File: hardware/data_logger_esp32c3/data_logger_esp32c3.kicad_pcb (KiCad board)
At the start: 2 copper layers, 43.4 x 55.4 mm, 48 parts, among them U1 ESP32-C3-MINI-1, U10 A03401A, U2 AZ1117IH-3.3TRG1, U3 LM321MF, U4 LM321MF, U5 LM321MF, U6 LM321MF, U7 LM321MF, U8 LM321MF, U9 A03401A

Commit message: More hardware work
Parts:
- moved U9 59.2 mm to (134.9, 88.2)
- moved U10 58.3 mm to (137.7, 82.5)
- moved TX0 19.3 mm to (124.7, 51.6)
- moved R1 14.5 mm to (126.4, 56.9), turned to 90 degrees
- moved RX0 14.4 mm to (124.7, 54.5)
- moved C3 11.3 mm to (106.4, 57.6), turned to 180 degrees
- moved R3 10.4 mm to (126.4, 54.9), turned to -90 degrees
- moved C1 2.82 mm to (105.9, 63.2), turned to -90 degrees
- moved R7 2.28 mm to (131.7, 69.1)
- moved U1 2.11 mm to (116.7, 58.2)
- moved SD1 1.63 mm to (134.1, 69.4)
- moved C2 1.06 mm to (106.1, 58.9), turned to 180 degrees
- moved R2 1.02 mm to (131.7, 72.0)
- moved USB-C1 0.88 mm to (129.1, 70.0)
- moved R4 0.83 mm to (107.1, 63.2), turned to 90 degrees
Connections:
- U1 pad 11: (no net) -> GND
- U1 pad 14: (no net) -> GND

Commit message: adding to hardware
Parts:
- added ?: TestPoint, TestPoint:TestPoint_THTPad_1.0x1.0mm_Drill0.5mm, F.Cu at (127.3, 76.1)
- added ?: TestPoint, TestPoint:TestPoint_THTPad_1.0x1.0mm_Drill0.5mm, F.Cu at (124.3, 76.1)
- moved ADC1-1 55.6 mm to (114.7, 75.8)
- moved ADC1+1 53.3 mm to (108.6, 75.9)
- moved U4 47.4 mm to (110.6, 65.8)
- moved C5 22.6 mm to (141.3, 79.7), turned to 90 degrees
- moved U2 16.8 mm to (136.8, 87.8), turned to 180 degrees
- moved U9 15.7 mm to (128.0, 74.2)
- moved U10 14.8 mm to (131.4, 69.1)
- moved DC-1 13.9 mm to (126.3, 83.4)
- moved R9 12.4 mm to (131.4, 76.7)
- moved DC+1 11.6 mm to (123.5, 83.4)
- moved C4 11.1 mm to (131.5, 78.1)
- moved D1 9.95 mm to (130.5, 79.4), turned to -90 degrees
- moved 3V3 7.06 mm to (140.6, 84.2)
- moved VIN1 6.45 mm to (131.6, 79.9)
- moved C3 2.86 mm to (109.2, 57.3), turned to 90 degrees
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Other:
- board size 43.4 x 55.4 mm -> 50 x 50 mm

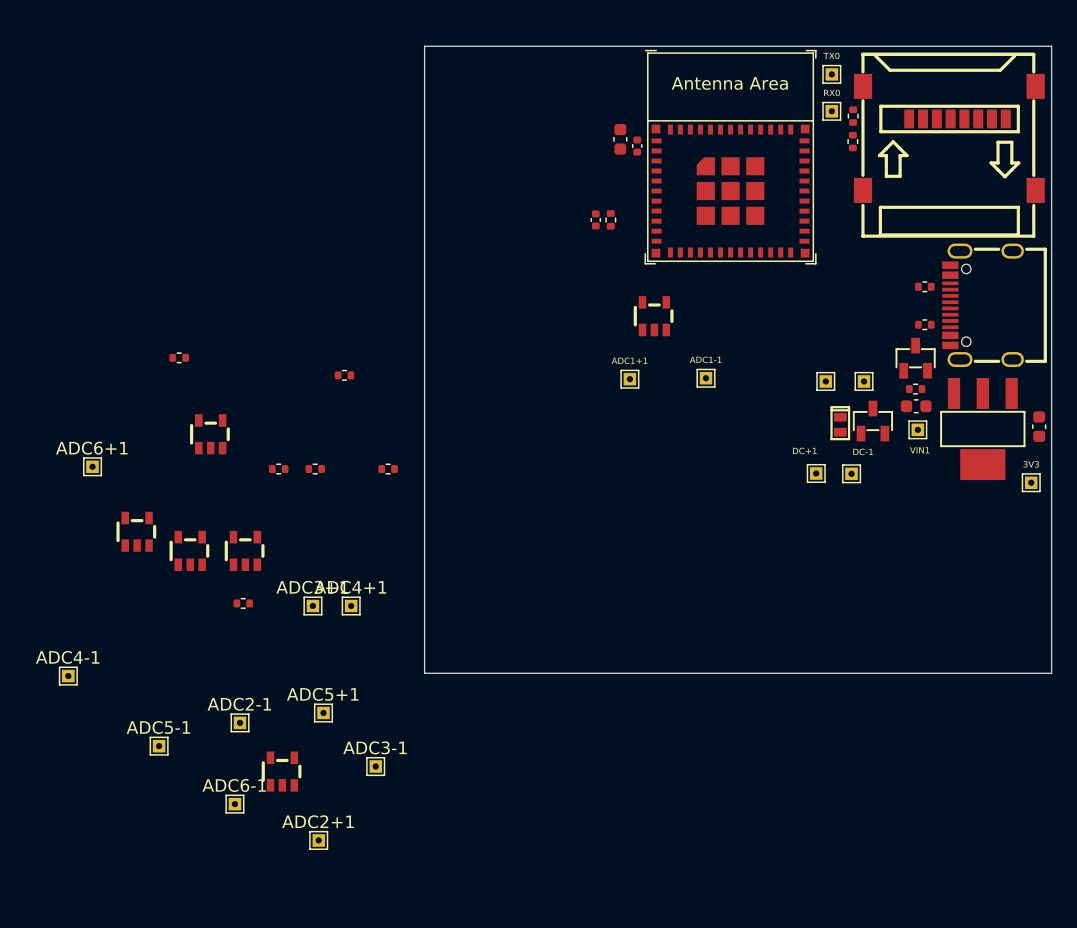
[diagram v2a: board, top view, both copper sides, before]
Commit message: Add gpio expander.  Layout complete
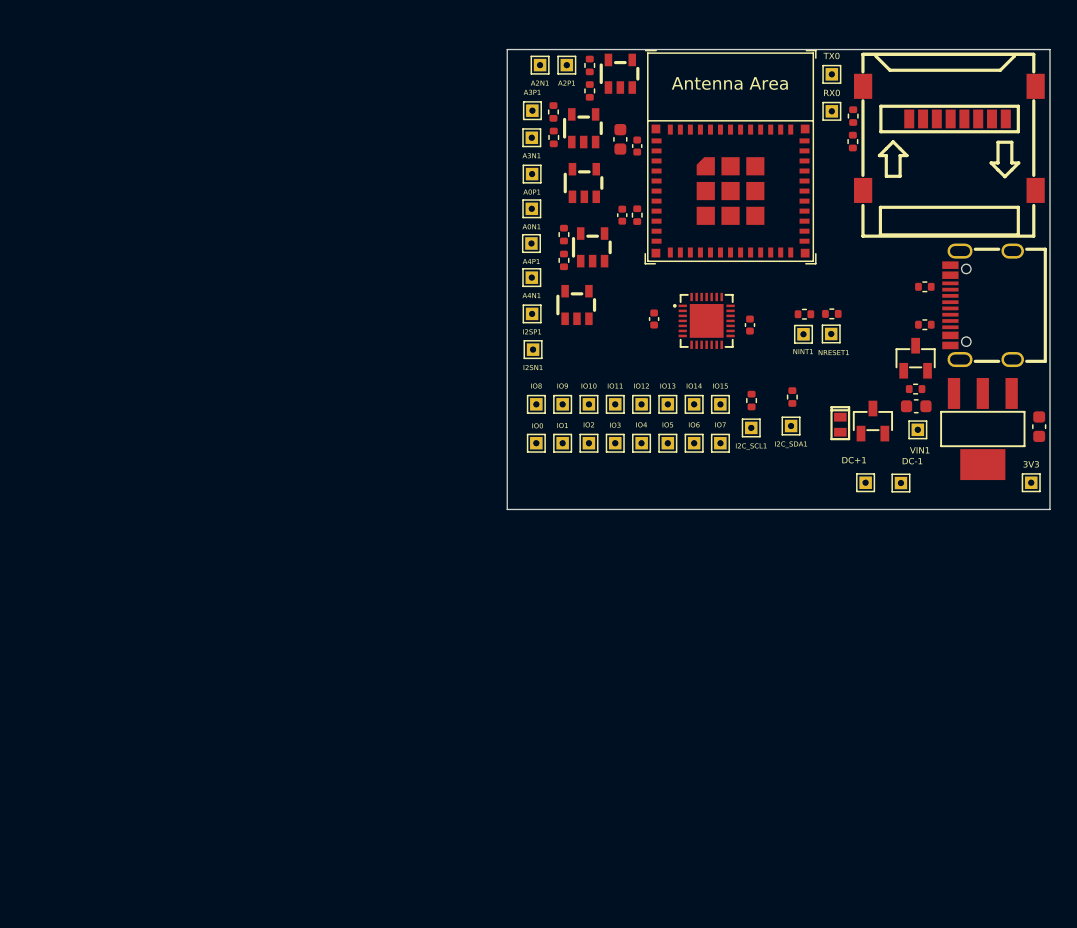
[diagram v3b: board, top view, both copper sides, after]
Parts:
- removed ? (x2), ADC1+1, ADC1-1, ADC2+1, ADC2-1, ADC3+1, ADC3-1, ADC4+1, ADC4-1, ADC5+1, ADC5-1, ADC6+1, ADC6-1: TestPoint, TestPoint:TestPoint_THTPad_1.0x1.0mm_Drill0.5mm
- removed U3: LM321MF, 1_project_footprints:LM321MF
- added A0N1: TestPoint, TestPoint:TestPoint_THTPad_1.0x1.0mm_Drill0.5mm, F.Cu at (100.8, 62.3)
- added A0P1: TestPoint, TestPoint:TestPoint_THTPad_1.0x1.0mm_Drill0.5mm, F.Cu at (100.8, 59.5)
- added A2N1: TestPoint, TestPoint:TestPoint_THTPad_1.0x1.0mm_Drill0.5mm, F.Cu at (101.5, 50.9)
- added A2P1: TestPoint, TestPoint:TestPoint_THTPad_1.0x1.0mm_Drill0.5mm, F.Cu at (103.6, 50.9)
- added A3N1: TestPoint, TestPoint:TestPoint_THTPad_1.0x1.0mm_Drill0.5mm, F.Cu at (100.8, 56.6)
- added A3P1: TestPoint, TestPoint:TestPoint_THTPad_1.0x1.0mm_Drill0.5mm, F.Cu at (100.9, 54.5)
- added A4N1: TestPoint, TestPoint:TestPoint_THTPad_1.0x1.0mm_Drill0.5mm, F.Cu at (100.8, 67.8)
- added A4P1: TestPoint, TestPoint:TestPoint_THTPad_1.0x1.0mm_Drill0.5mm, F.Cu at (100.8, 65.1)
- added C6: 0.1uF, Capacitor_SMD:C_0402_1005Metric, F.Cu at (118.2, 71.6)
- added C7: 0.1uF, Capacitor_SMD:C_0402_1005Metric, F.Cu at (110.6, 71.1)
- added I2C_SCL1: TestPoint, TestPoint:TestPoint_THTPad_1.0x1.0mm_Drill0.5mm, F.Cu at (118.3, 79.8)
- added I2C_SDA1: TestPoint, TestPoint:TestPoint_THTPad_1.0x1.0mm_Drill0.5mm, F.Cu at (121.5, 79.6)
- added I2SN1: TestPoint, TestPoint:TestPoint_THTPad_1.0x1.0mm_Drill0.5mm, F.Cu at (100.9, 73.5)
- added I2SP1: TestPoint, TestPoint:TestPoint_THTPad_1.0x1.0mm_Drill0.5mm, F.Cu at (100.8, 70.7)
- added IO0: TestPoint, TestPoint:TestPoint_THTPad_1.0x1.0mm_Drill0.5mm, F.Cu at (101.2, 81.0)
- added IO1: TestPoint, TestPoint:TestPoint_THTPad_1.0x1.0mm_Drill0.5mm, F.Cu at (103.3, 81.0)
- added IO10: TestPoint, TestPoint:TestPoint_THTPad_1.0x1.0mm_Drill0.5mm, F.Cu at (105.4, 77.9)
- added IO11: TestPoint, TestPoint:TestPoint_THTPad_1.0x1.0mm_Drill0.5mm, F.Cu at (107.5, 77.9)
- added IO12: TestPoint, TestPoint:TestPoint_THTPad_1.0x1.0mm_Drill0.5mm, F.Cu at (109.6, 77.9)
- added IO13: TestPoint, TestPoint:TestPoint_THTPad_1.0x1.0mm_Drill0.5mm, F.Cu at (111.7, 77.9)
- added IO14: TestPoint, TestPoint:TestPoint_THTPad_1.0x1.0mm_Drill0.5mm, F.Cu at (113.8, 77.9)
- added IO15: TestPoint, TestPoint:TestPoint_THTPad_1.0x1.0mm_Drill0.5mm, F.Cu at (115.9, 77.9)
- added IO2: TestPoint, TestPoint:TestPoint_THTPad_1.0x1.0mm_Drill0.5mm, F.Cu at (105.4, 81.0)
- added IO3: TestPoint, TestPoint:TestPoint_THTPad_1.0x1.0mm_Drill0.5mm, F.Cu at (107.5, 81.0)
- added IO4: TestPoint, TestPoint:TestPoint_THTPad_1.0x1.0mm_Drill0.5mm, F.Cu at (109.6, 81.0)
- added IO5: TestPoint, TestPoint:TestPoint_THTPad_1.0x1.0mm_Drill0.5mm, F.Cu at (111.7, 81.0)
- added IO6: TestPoint, TestPoint:TestPoint_THTPad_1.0x1.0mm_Drill0.5mm, F.Cu at (113.8, 81.0)
- added IO7: TestPoint, TestPoint:TestPoint_THTPad_1.0x1.0mm_Drill0.5mm, F.Cu at (115.9, 81.0)
- added IO8: TestPoint, TestPoint:TestPoint_THTPad_1.0x1.0mm_Drill0.5mm, F.Cu at (101.2, 77.9)
- added IO9: TestPoint, TestPoint:TestPoint_THTPad_1.0x1.0mm_Drill0.5mm, F.Cu at (103.3, 77.9)
- added NINT1: TestPoint, TestPoint:TestPoint_THTPad_1.0x1.0mm_Drill0.5mm, F.Cu at (122.5, 72.3)
- added NRESET1: TestPoint, TestPoint:TestPoint_THTPad_1.0x1.0mm_Drill0.5mm, F.Cu at (124.7, 72.3)
- added R14: 10k, Resistor_SMD:R_0402_1005Metric, F.Cu at (124.7, 70.7)
- added R15: 10k, Resistor_SMD:R_0402_1005Metric, F.Cu at (122.6, 70.7)
- added R16: 4.7k, Resistor_SMD:R_0402_1005Metric, F.Cu at (121.6, 77.3)
- added R8: 4.7k, Resistor_SMD:R_0402_1005Metric, F.Cu at (118.3, 77.6)
- added U11: SX1509BIULTRT, 1_project_footprints:QFN-28-EP(4x4), F.Cu at (119.6, 71.2)
- moved R13 49.3 mm to (105.4, 52.9), turned to -90 degrees
- moved U5 48.4 mm to (107.9, 46.5)
- moved R10 40.6 mm to (105.4, 50.9), turned to -90 degrees
- moved U7 40.2 mm to (105.7, 60.3)
- moved U8 39.5 mm to (104.4, 64.9)
- moved U6 38.5 mm to (105.0, 50.8)
- moved R6 31.7 mm to (103.4, 66.4), turned to -90 degrees
- moved R11 31.4 mm to (102.5, 54.6), turned to -90 degrees
- moved R12 27.3 mm to (103.4, 64.4), turned to -90 degrees
- moved R5 25.3 mm to (102.6, 56.6), turned to -90 degrees
- moved U4 12.0 mm to (105.0, 55.2)
- moved DC-1 4.01 mm to (130.3, 84.2)
- moved DC+1 4.01 mm to (127.4, 84.2)
- moved C1 2.14 mm to (108.0, 62.8)
- moved R4 2.14 mm to (109.2, 62.8)
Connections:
- U1 pad 13: ADC1_CH1 -> I2C_SDA
- U1 pad 16: unconnected-(U1-Pad16) -> I2C_SCL
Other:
- board size 50 x 50 mm -> 43.3 x 36.7 mm

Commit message: more layout
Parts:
- removed I2C_SCL1, I2C_SDA1: TestPoint, TestPoint:TestPoint_THTPad_1.0x1.0mm_Drill0.5mm
- added SCL1: TestPoint, TestPoint:TestPoint_THTPad_1.0x1.0mm_Drill0.5mm, F.Cu at (117.7, 79.7)
- added SDA1: TestPoint, TestPoint:TestPoint_THTPad_1.0x1.0mm_Drill0.5mm, F.Cu at (119.9, 79.8)
- moved VIN1 14.9 mm to (126.5, 66.0)
- moved 3V3 13.4 mm to (127.9, 80.0)
- moved C5 13.2 mm to (129.0, 74.8)
- moved U2 12.9 mm to (124.6, 83.6)
- moved C4 12.2 mm to (129.8, 66.0), turned to 0 degrees
- moved DC+1 11.4 mm to (137.8, 79.5)
- moved DC-1 11.0 mm to (140.2, 79.5)
- moved D1 10.9 mm to (138.9, 72.4), turned to 0 degrees
- moved R9 9.40 mm to (129.7, 67.4), turned to 180 degrees
- moved U9 9.27 mm to (132.0, 82.5), turned to 180 degrees
- moved NINT1 5.96 mm to (117.4, 75.5)
- moved R14 5.96 mm to (119.7, 73.9)
- moved R15 5.96 mm to (117.5, 73.9)
- moved NRESET1 5.96 mm to (119.7, 75.5)
- moved U10 3.39 mm to (134.7, 70.1), turned to -90 degrees
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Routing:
- added copper zone on In1.Cu, net +3V3
- added copper zone on In2.Cu, net GND
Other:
- board size 43.3 x 36.7 mm -> 43.3 x 32.3 mm
- copper layers 2 -> 4

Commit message: commit before routing
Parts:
- added R17: 30.1, Resistor_SMD:R_0402_1005Metric, F.Cu at (124.6, 63.3)
- added R18: 30.1, Resistor_SMD:R_0402_1005Metric, F.Cu at (124.6, 64.4)
- moved VIN1 15.0 mm to (130.2, 80.5), turned to -90 degrees
- moved 3V3 0.43 mm to (127.9, 80.5)
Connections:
- USB-C1 pad A6: D+ -> Net-(USB-C1-PadA6)
- USB-C1 pad A7: D- -> Net-(USB-C1-PadA7)
- USB-C1 pad B6: D+ -> Net-(USB-C1-PadA6)
- USB-C1 pad B7: D- -> Net-(USB-C1-PadA7)
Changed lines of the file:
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@@
   (net 68 "Net-(A4P1-Pad1)")
   (net 69 "Net-(I2SP1-Pad1)")
+  (net 70 "Net-(USB-C1-PadA6)")
+  (net 71 "Net-(USB-C1-PadA7)")
   (footprint "1_project_footprints:LM321MF" (layer "F.Cu")
     (at 107.873813 46.456944)
@@
   )
   (footprint "TestPoint:TestPoint_THTPad_1.0x1.0mm_Drill0.5mm" (layer "F.Cu")
-    (at 126.5174 65.9638)
+    (at 130.175 80.518 -90)
     (descr "THT rectangular pad as test Point, square 1.0mm side length, hole diameter 0.5mm")
     (tags "test point THT pad rectangle square")
@@
     (property "Sheetname" "")
     (attr exclude_from_pos_files)
-    (fp_text reference "VIN1" (at -1.4986 0.0508 90) (layer "F.SilkS")
+    (fp_text reference "VIN1" (at -1.4986 0.0508) (layer "F.SilkS")
       (effects (font (size 0.5 0.5) (thickness 0.125)))
     )
-    (fp_text value "TestPoint" (at 0 1.55) (layer "F.Fab")
-      (effects (font (size 1 1) (thickness 0.15)))
-    )
-    (fp_text user "${REFERENCE}" (at 0 -1.45) (layer "F.Fab")
+    (fp_text value "TestPoint" (at 0 1.55 90) (layer "F.Fab")
+      (effects (font (size 1 1) (thickness 0.15)))
+    )
+    (fp_text user "${REFERENCE}" (at 0 -1.45 90) (layer "F.Fab")
       (effects (font (size 1 1) (thickness 0.15)))
     )
@@
     (fp_line (start 1 1) (end 1 -1) (layer "F.CrtYd") (width 0.05))
     (fp_line (start -1 -1) (end 1 -1) (layer "F.CrtYd") (width 0.05))
-    (pad "1" thru_hole rect (at 0 0) (size 1 1) (drill 0.5) (layers *.Cu *.Mask)
+    (pad "1" thru_hole rect (at 0 0 270) (size 1 1) (drill 0.5) (layers *.Cu *.Mask)
       (net 39 "Net-(C4-Pad1)") (pinfunction "1") (pintype "passive"))
   )
@@
   )
   (footprint "Resistor_SMD:R_0402_1005Metric" (layer "F.Cu")
+    (at 124.6124 64.3636)
+    (descr "Resistor SMD 0402 (1005 Metric), square (rectangular) end terminal, IPC_7351 nominal, (Body size source: IPC-SM-782 page 72, https://www.pcb-3d.com/wordpress/wp-content/uploads/ipc-sm-782a_amendment_1_and_2.pdf), generated with kicad-footprint-generator")
+    (tags "resistor")
+    (property "Sheetfile" "data_logger_esp32c3.kicad_sch")
+    (property "Sheetname" "")
+    (property "part_number" "0402WGF301JTCE")
+    (attr smd)
+    (fp_text reference "R18" (at -0.4572 0.9144) (layer "F.SilkS")
+      (effects (font (size 0.4 0.4) (thickness 0.1)))
+    )
+    (fp_text value "30.1" (at 0 1.17) (layer "F.Fab")
+      (effects (font (size 1 1) (thickness 0.15)))
+    )
+    (fp_text user "${REFERENCE}" (at 0 0) (layer "F.Fab")
+      (effects (font (size 0.26 0.26) (thickness 0.04)))
+    )
+    (fp_line (start -0.153641 -0.38) (end 0.153641 -0.38) (layer "F.SilkS") (width 0.12))
+    (fp_line (start -0.153641 0.38) (end 0.153641 0.38) (layer "F.SilkS") (width 0.12))
+    (fp_line (start 0.93 -0.47) (end 0.93 0.47) (layer "F.CrtYd") (width 0.05))
+    (fp_line (start -0.93 0.47) (end -0.93 -0.47) (layer "F.CrtYd") (width 0.05))
+    (fp_line (start -0.93 -0.47) (end 0.93 -0.47) (layer "F.CrtYd") (width 0.05))
+    (fp_line (start 0.93 0.47) (end -0.93 0.47) (layer "F.CrtYd") (width 0.05))
+    (fp_line (start -0.525 -0.27) (end 0.525 -0.27) (layer "F.Fab") (width 0.1))
+    (fp_line (start -0.525 0.27) (end -0.525 -0.27) (layer "F.Fab") (width 0.1))
+    (fp_line (start 0.525 -0.27) (end 0.525 0.27) (layer "F.Fab") (width 0.1))
+    (fp_line (start 0.525 0.27) (end -0.525 0.27) (layer "F.Fab") (width 0.1))
+    (pad "1" smd roundrect (at -0.51 0) (size 0.54 0.64) (layers "F.Cu" "F.Paste" "F.Mask") (roundrect_rratio 0.25)
+      (net 18 "D-") (pintype "passive"))
+    (pad "2" smd roundrect (at 0.51 0) (size 0.54 0.64) (layers "F.Cu" "F.Paste" "F.Mask") (roundrect_rratio 0.25)
+      (net 71 "Net-(USB-C1-PadA7)") (pintype "passive"))
+    (model "${KICAD6_3DMODEL_DIR}/Resistor_SMD.3dshapes/R_0402_1005Metric.wrl"
+      (offset (xyz 0 0 0))
+      (scale (xyz 1 1 1))
+      (rotate (xyz 0 0 0))
+    )
+  )
+  (footprint "Resistor_SMD:R_0402_1005Metric" (layer "F.Cu")
     (at 103.378 66.421 -90)
     (descr "Resistor SMD 0402 (1005 Metric), square (rectangular) end terminal, IPC_7351 nominal, (Body size source: IPC-SM-782 page 72, https://www.pcb-3d.com/wordpress/wp-content/uploads/ipc-sm-782a_amendment_1_and_2.pdf), generated with kicad-footprint-generator")
@@
     (pad "1" thru_hole rect (at 0 0 180) (size 1 1) (drill 0.5) (layers *.Cu *.Mask)
       (net 2 "GND") (pinfunction "1") (pintype "passive"))
+  )
+  (footprint "Resistor_SMD:R_0402_1005Metric" (layer "F.Cu")
+    (at 124.587 63.2714)
+    (descr "Resistor SMD 0402 (1005 Metric), square (rectangular) end terminal, IPC_7351 nominal, (Body size source: IPC-SM-782 page 72, https://www.pcb-3d.com/wordpress/wp-content/uploads/ipc-sm-782a_amendment_1_and_2.pdf), generated with kicad-footprint-generator")
+    (tags "resistor")
+    (property "Sheetfile" "data_logger_esp32c3.kicad_sch")
+    (property "Sheetname" "")
+    (property "part_number" "0402WGF301JTCE")
+    (attr smd)
+    (fp_text reference "R17" (at 0 -0.8636) (layer "F.SilkS")
+      (effects (font (size 0.4 0.4) (thickness 0.1)))
+    )
+    (fp_text value "30.1" (at 0 1.17) (layer "F.Fab")
+      (effects (font (size 1 1) (thickness 0.15)))
+    )
+    (fp_text user "${REFERENCE}" (at 0 0) (layer "F.Fab")
+      (effects (font (size 0.26 0.26) (thickness 0.04)))
+    )
+    (fp_line (start -0.153641 -0.38) (end 0.153641 -0.38) (layer "F.SilkS") (width 0.12))
+    (fp_line (start -0.153641 0.38) (end 0.153641 0.38) (layer "F.SilkS") (width 0.12))
+    (fp_line (start -0.93 0.47) (end -0.93 -0.47) (layer "F.CrtYd") (width 0.05))
+    (fp_line (start 0.93 0.47) (end -0.93 0.47) (layer "F.CrtYd") (width 0.05))
+    (fp_line (start -0.93 -0.47) (end 0.93 -0.47) (layer "F.CrtYd") (width 0.05))
+    (fp_line (start 0.93 -0.47) (end 0.93 0.47) (layer "F.CrtYd") (width 0.05))
+    (fp_line (start -0.525 -0.27) (end 0.525 -0.27) (layer "F.Fab") (width 0.1))
+    (fp_line (start -0.525 0.27) (end -0.525 -0.27) (layer "F.Fab") (width 0.1))
+    (fp_line (start 0.525 0.27) (end -0.525 0.27) (layer "F.Fab") (width 0.1))
+    (fp_line (start 0.525 -0.27) (end 0.525 0.27) (layer "F.Fab") (width 0.1))
+    (pad "1" smd roundrect (at -0.51 0) (size 0.54 0.64) (layers "F.Cu" "F.Paste" "F.Mask") (roundrect_rratio 0.25)
+      (net 17 "D+") (pintype "passive"))
+    (pad "2" smd roundrect (at 0.51 0) (size 0.54 0.64) (layers "F.Cu" "F.Paste" "F.Mask") (roundrect_rratio 0.25)
+      (net 70 "Net-(USB-C1-PadA6)") (pintype "passive"))
+    (model "${KICAD6_3DMODEL_DIR}/Resistor_SMD.3dshapes/R_0402_1005Metric.wrl"
+      (offset (xyz 0 0 0))
+      (scale (xyz 1 1 1))
+      (rotate (xyz 0 0 0))
+    )
   )
   (footprint "1_espressif:ESP32-C3-MINI-1" (layer "F.Cu")
@@
   )
   (footprint "TestPoint:TestPoint_THTPad_1.0x1.0mm_Drill0.5mm" (layer "F.Cu")
-    (at 127.9144 80.0354)
+    (at 127.9144 80.4672)
     (descr "THT rectangular pad as test Point, square 1.0mm side length, hole diameter 0.5mm")
     (tags "test point THT pad rectangle square")
@@
       (net 36 "Net-(R2-Pad2)") (pinfunction "CC1") (pintype "bidirectional"))
     (pad "A6" smd rect (at -0.249936 5.13588 90) (size 0.299999 1.299997) (layers "F.Cu" "F.Paste" "F.Mask")
-      (net 17 "D+") (pinfunction "DP1") (pintype "bidirectional"))
+      (net 70 "Net-(USB-C1-PadA6)") (pinfunction "DP1") (pintype "bidirectional"))
     (pad "A7" smd rect (at 0.249936 5.13588 90) (size 0.299999 1.299997) (layers "F.Cu" "F.Paste" "F.Mask")
-      (net 18 "D-") (pinfunction "DN1") (pintype "bidirectional"))
+      (net 71 "Net-(USB-C1-PadA7)") (pinfunction "DN1") (pintype "bidirectional"))
     (pad "A8" smd rect (at 1.24968 5.13588 90) (size 0.299999 1.299997) (layers "F.Cu" "F.Paste" "F.Mask")
       (net 19 "unconnected-(USB-C1-PadA8)") (pinfunction "SBU1") (pintype "bidirectional+no_connect"))
@@
       (net 37 "Net-(R7-Pad2)") (pinfunction "CC2") (pintype "bidirectional"))
     (pad "B6" smd rect (at 0.750062 5.13588 90) (size 0.299999 1.299997) (layers "F.Cu" "F.Paste" "F.Mask")
-      (net 17 "D+") (pinfunction "DP2") (pintype "bidirectional"))
+      (net 70 "Net-(USB-C1-PadA6)") (pinfunction "DP2") (pintype "bidirectional"))
     (pad "B7" smd rect (at -0.750062 5.13588 90) (size 0.299999 1.299997) (layers "F.Cu" "F.Paste" "F.Mask")
-      (net 18 "D-") (pinfunction "DN2") (pintype "bidirectional"))
+      (net 71 "Net-(USB-C1-PadA7)") (pinfunction "DN2") (pintype "bidirectional"))
     (pad "B8" smd rect (at -1.75006 5.13588 90) (size 0.299999 1.299997) (layers "F.Cu" "F.Paste" "F.Mask")
       (net 20 "unconnected-(USB-C1-PadB8)") (pinfunction "SBU2") (pintype "bidirectional+no_connect"))
